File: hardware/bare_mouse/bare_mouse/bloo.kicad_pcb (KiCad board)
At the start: 2 copper layers, 94 x 99.8 mm, 101 parts, among them J1 Serial Debug Header, J10 Conn_01x06_Female, J2 SWD Header, J4 Conn_ARM_JTAG_SWD_10, J5 SWD Header, M1 M1_Conn_Alt, M2 M2_Conn_Alt, Q0 TEFT4300, Q1 TEFT4300, Q10 Q_NMOS_GSD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

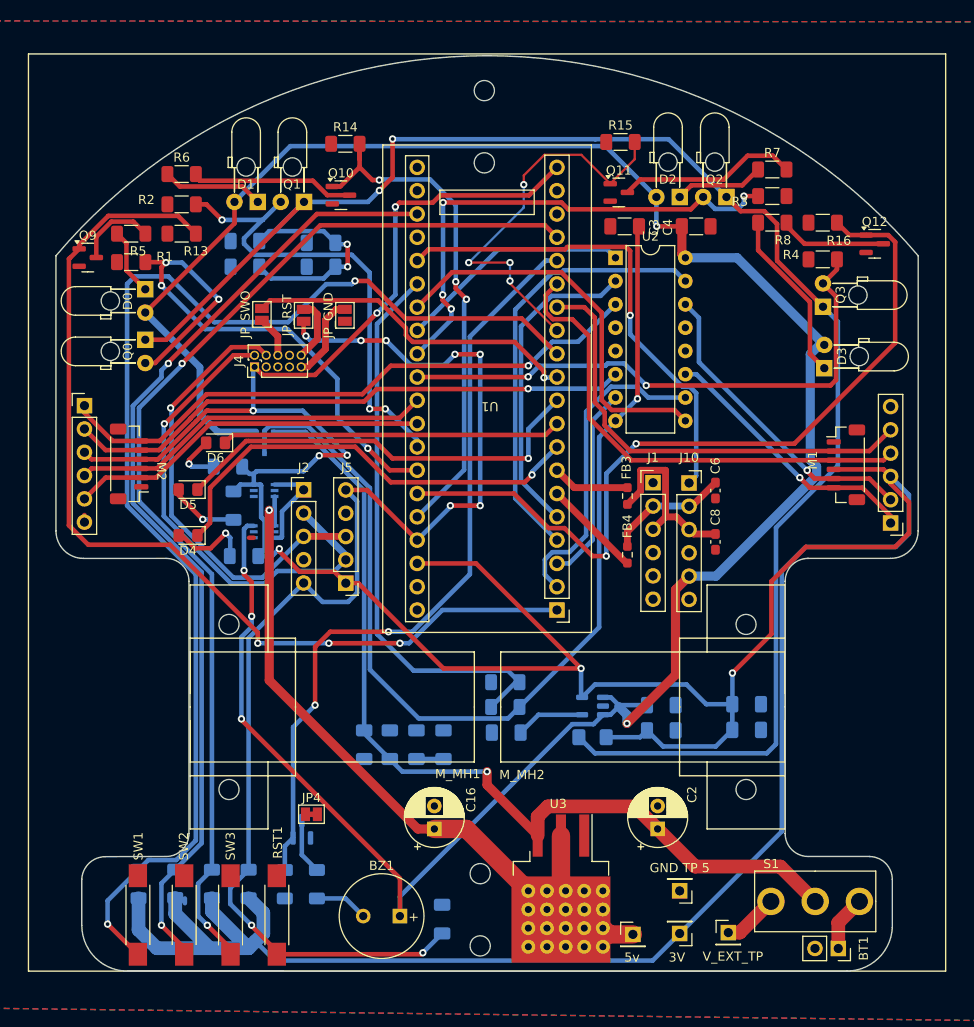
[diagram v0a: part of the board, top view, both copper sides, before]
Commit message: resolved outlines issue and added some vias to fix grounding planes
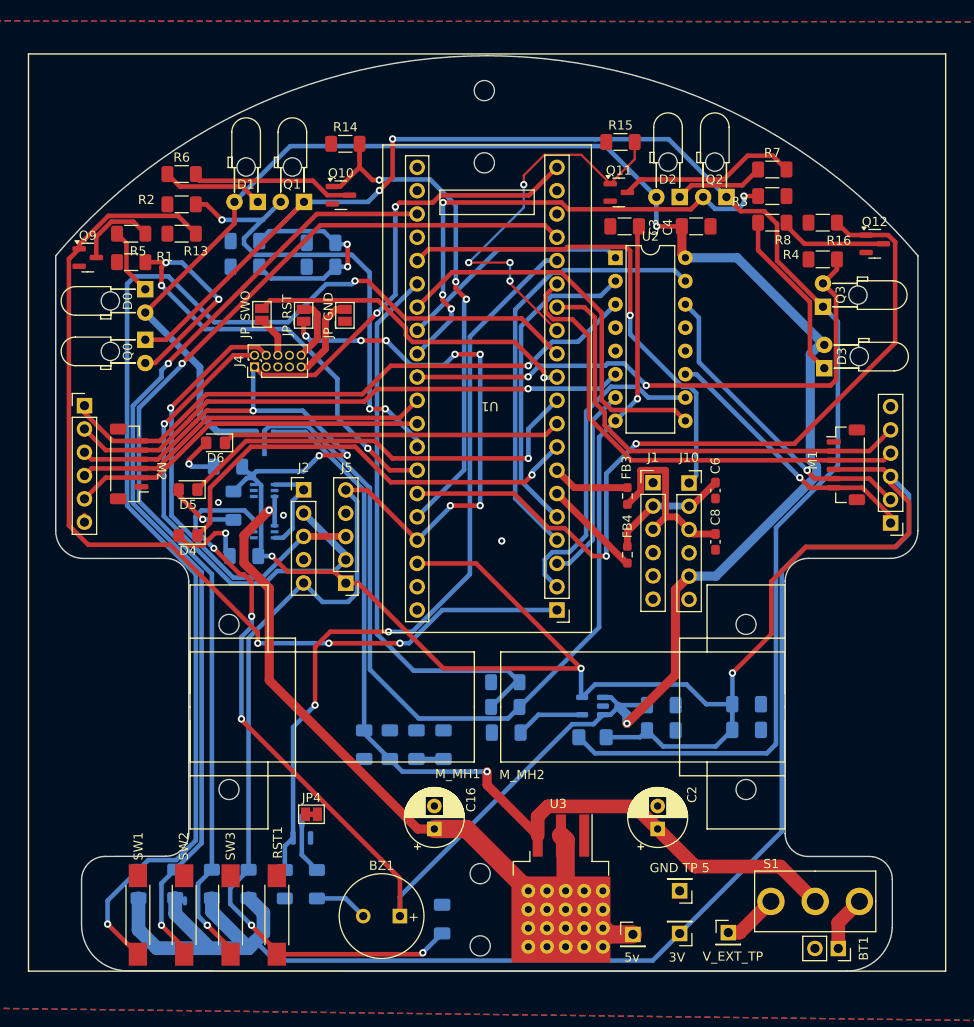
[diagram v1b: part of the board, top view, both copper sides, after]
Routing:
- net +5V: track 262.2 -> 272.5 mm
- net +5V_NET: track 78.6 -> 75.1 mm
- net +3V3: track 413.4 -> 412.1 mm
- net GND: vias 0 -> 3
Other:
- outline, holes or cut-outs redrawn

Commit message: oopsies didnt save last time
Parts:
- removed BT_MH1, BT_MH2, BT_MH3, BT_MH4: M2, MountingHole:MountingHole_2.2mm_M2
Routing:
- net +3V3: track 412.1 -> 414.7 mm
- net GND: vias 3 -> 4

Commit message: changes after meeting with eaton
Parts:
- moved C12 133.5 mm to (241.7, 178.7)
- moved C18 133.5 mm to (241.7, 175.9)
- moved R20 132.5 mm to (186.9, 153.7)
- moved R23 131.5 mm to (217.6, 172.8)
- moved D4 131.4 mm to (183.0, 157.1)
- moved BT1 131.3 mm to (253.9, 202.5)
- moved C19 131.3 mm to (210.7, 199.3)
- moved C2 131.3 mm to (234.2, 189.5)
- moved C20 131.3 mm to (189.2, 125.4)
- moved C21 131.3 mm to (189.2, 128.2)
- moved J1 131.3 mm to (233.7, 151.8)
- moved J5 131.3 mm to (200.2, 162.7)
- moved JP4 131.3 mm to (196.4, 187.9)
- moved M1 131.3 mm to (262.8, 149.2)
- moved Q1 131.3 mm to (195.6, 121.1)
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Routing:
- net GND: track 0.78 -> 10.7 mm
- net +5V: track 272.5 -> 269.3 mm, vias 5 -> 6
- net +5V_NET: track 75.1 -> 72.2 mm
- net BATT_NET: track 100.8 -> 102.9 mm
- net VCC: track 113.6 -> 114.9 mm
- net 3V3_BYP: track 7.52 -> 8.69 mm
- net +3.3VA: track 199.6 -> 198.4 mm
- net +3V3: track 414.7 -> 413.6 mm, vias 8 -> 7
- net Net-(D4-A): track 9.26 -> 8.24 mm
- net SWDIO: track 54.0 -> 55.0 mm
- net RECEIV_2: track 51.4 -> 52.0 mm
- net EMIT_1: track 106.9 -> 107.5 mm

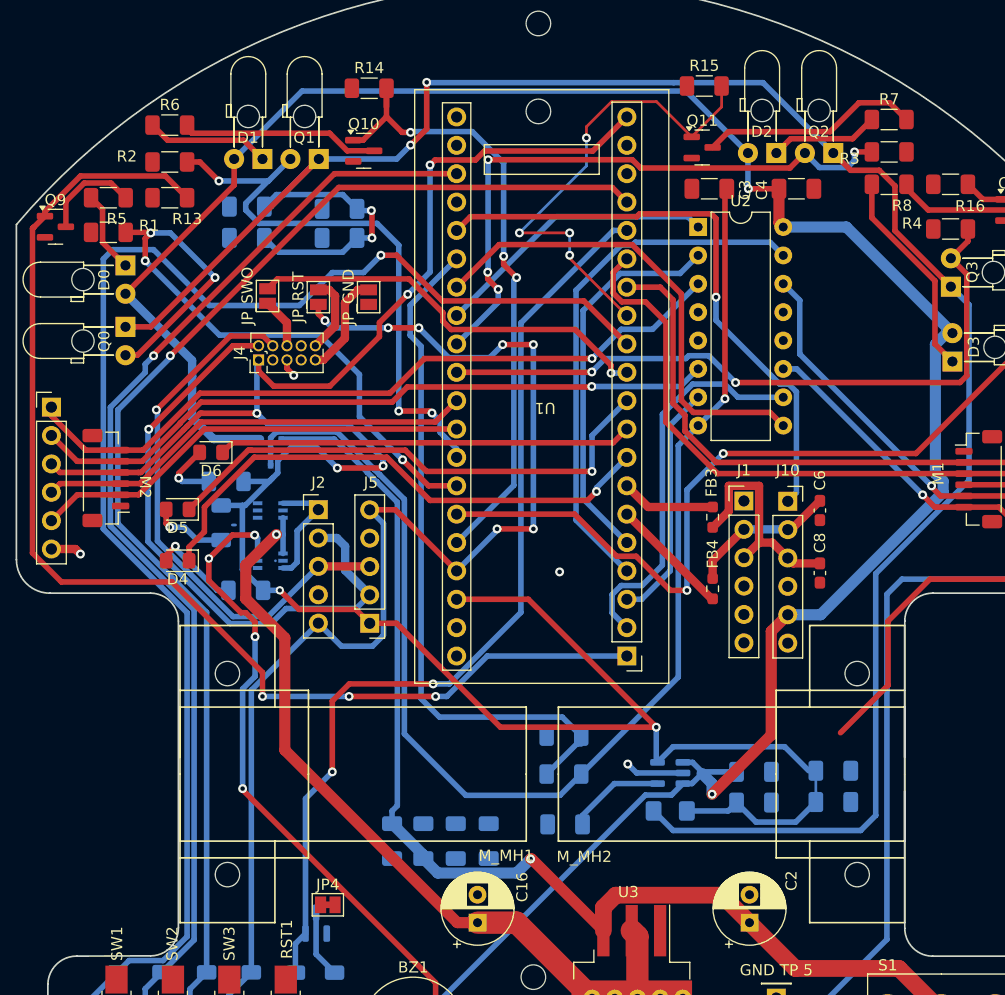
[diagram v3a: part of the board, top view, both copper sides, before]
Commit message: errors resolved. JP4 too far away from capacitors?
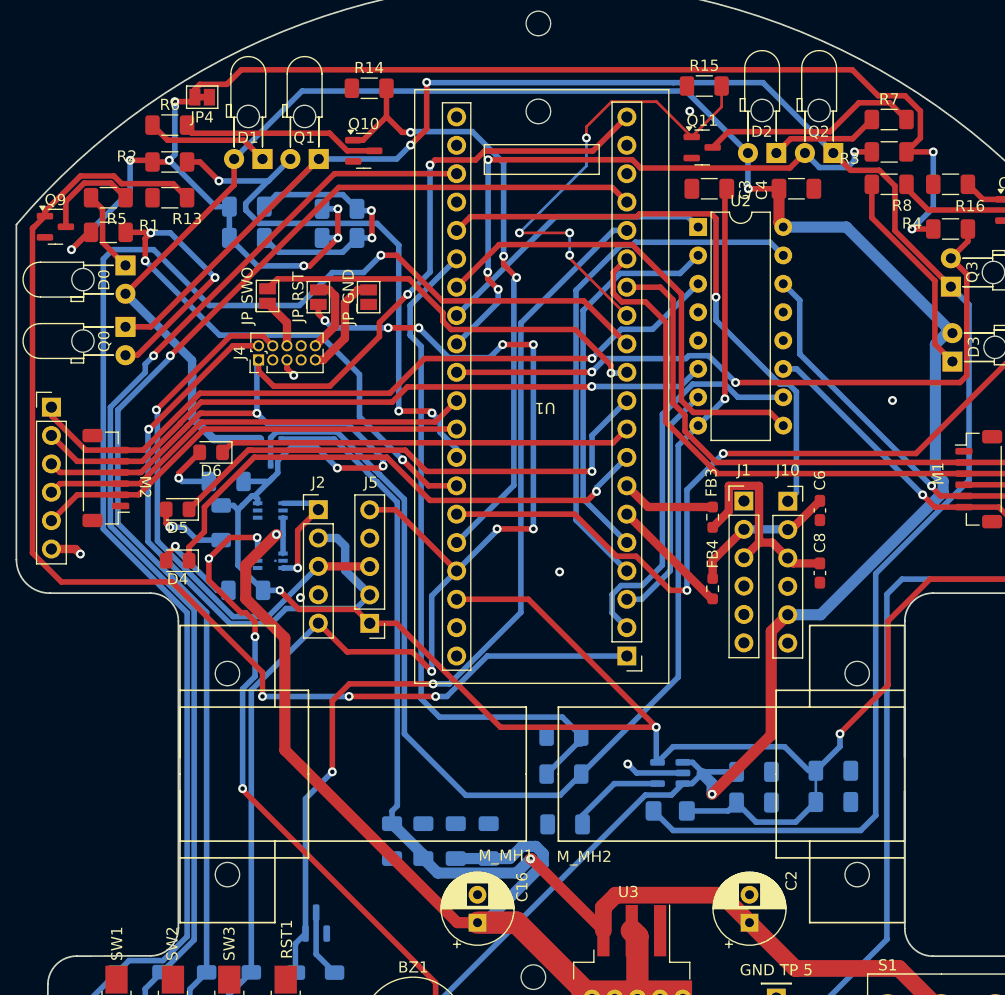
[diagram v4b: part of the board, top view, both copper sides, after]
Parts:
- moved JP4 73.2 mm to (185.2, 115.6), turned to 180 degrees
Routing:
- net AGND: track 0.00 -> 134.8 mm, vias 0 -> 9
- net +5V_NET: track 72.2 -> 89.7 mm
- net +3V3: track 413.6 -> 418.8 mm, vias 7 -> 8
- net RST: track 141.0 -> 144.0 mm, vias 9 -> 10
- net EMIT_2: track 57.0 -> 55.3 mm
- net +3V3_NET: track 10.4 -> 10.7 mm, vias 0 -> 1
- net GND: track 10.7 -> 10.4 mm, vias 4 -> 7

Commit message: added most important part
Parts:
- added G***: LOGO, LOGO, B.Cu at (194.6, 173.0)
- GND: renamed from GND TP 5
- moved BT1 0.98 mm to (253.0, 202.9)
- moved M_MH2 0.34 mm to (216.8, 176.2)
- moved M_MH1 0.14 mm to (214.3, 176.2)
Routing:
- net +5V: track 269.1 -> 265.4 mm, vias 6 -> 5
- net Net-(BT1-+): track 6.09 -> 6.88 mm

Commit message: added team names to back silkscreen
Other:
- board text added: "Adam Wu Jeremiah Yong Jayce Spurgiasz"
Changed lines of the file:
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@@
 	)
 	(gr_text "Muad' Dib Desert Mice"
-		(at 249.4 132.3 90)
+		(at 243.6 132.4 90)
 		(layer "B.SilkS")
 		(effects
@@
 			)
 			(justify left bottom mirror)
+		)
+	)
+	(gr_text "Adam Wu\nJeremiah Yong\nJayce Spurgiasz"
+		(at 249.3 132.7 90)
+		(layer "B.SilkS")
+		(effects
+			(font
+				(size 1 1)
+				(thickness 0.15)
+			)
+			(justify left bottom mirror)
